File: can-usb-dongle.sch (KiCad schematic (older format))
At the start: 39 parts, among them SW1 SW_PUSH, U1 STM32F302C8T, U2 SN65HVD256, U3 MCP1700, U4 SiP32431, X1 16MHz 10ppm

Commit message: Rearrange symbols.
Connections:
- wire segments 129 -> 128
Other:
- moved on the sheet: C10, C7, C8, C9, C?, CONN1, CONN2, CONN?, D2, D3, D?, F1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

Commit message: Start with footrpint placement on PCB
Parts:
- removed CONN2: UART, symbol UART
- added CONN1: UART, _connectors:Molex-PicoBlade-4, symbol CONN_01X04
- added R10, R11: 100, _std:_0603, symbol R
- C1, C2, C3, C4, C6, C7, C8: footprint Capacitors_SMD:C_0603_HandSoldering -> _std:_0603
- C10, C13, C14, C9: renamed from C?; footprint (none) -> _std:_0603
- C11: renamed from C9; footprint Capacitors_SMD:C_0603_HandSoldering -> _std:_0603
- C12: renamed from C10; footprint Capacitors_SMD:C_0603_HandSoldering -> _std:_0603
- C5: value 100n -> 100nF; footprint Capacitors_SMD:C_0603_HandSoldering -> _std:_0603
- CONN2: renamed from CONN1; footprint (none) -> _connectors:_Solder_Pad1.27_5
- CONN3: renamed from CONN?; footprint (none) -> _connectors:_Micro-USB-AB-receptacle-SMT-th
- CONN4: renamed from CONN3; footprint Connectors_Molex:Connector_Molex_PicoBlade_53261-0471 -> _connectors:_Molex-PicoBlade-SMD-4
- CONN5: renamed from CONN4; footprint Connectors_Molex:Connector_Molex_PicoBlade_53261-0471 -> _connectors:_Molex-PicoBlade-SMD-4
- D1: renamed from D2; footprint LEDs:LED-0603 -> _std:_0603
- D2: renamed from D3; footprint LEDs:LED-0603 -> _std:_0603
- D3: renamed from D?; footprint LEDs:LED-0603 -> _std:_0603
- F1: footprint Resistors_SMD:R_0805_HandSoldering -> _std:_0603
- R1, R2, R5, R6: footprint Resistors_SMD:R_0603 -> _std:_0603
- R3, R4, R8: renamed from R?; footprint (none) -> _std:_0603
- R7: renamed from R?; footprint Resistors_SMD:R_0603 -> _std:_0603
- R9: renamed from R7; footprint Resistors_SMD:R_0603 -> _std:_0603
- SW1: footprint (none) -> _div:PushButtonSMD-5x3mm
- U2: footprint Transistors_SMD:sc70-5 -> Housings_SOIC:SOIC-8_3.9x4.9mm_Pitch1.27mm
- U3: renamed from U?; footprint (none) -> _std:SOT-563_6-lead
- U5: renamed from U4; footprint (none) -> Housings_SOT-23_SOT-143_TSOT-6:SC-70-6
- X1: footprint (none) -> _div:_TSX-3225-SMD-XTAL
- renumbered U3 to U4
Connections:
- wire segments 128 -> 100
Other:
- note added: "(5V tolerant)"
- note removed: "5V tolerant"
- note removed: "PREVIEW VERSION!\nPINOUT CAN CHANGE"

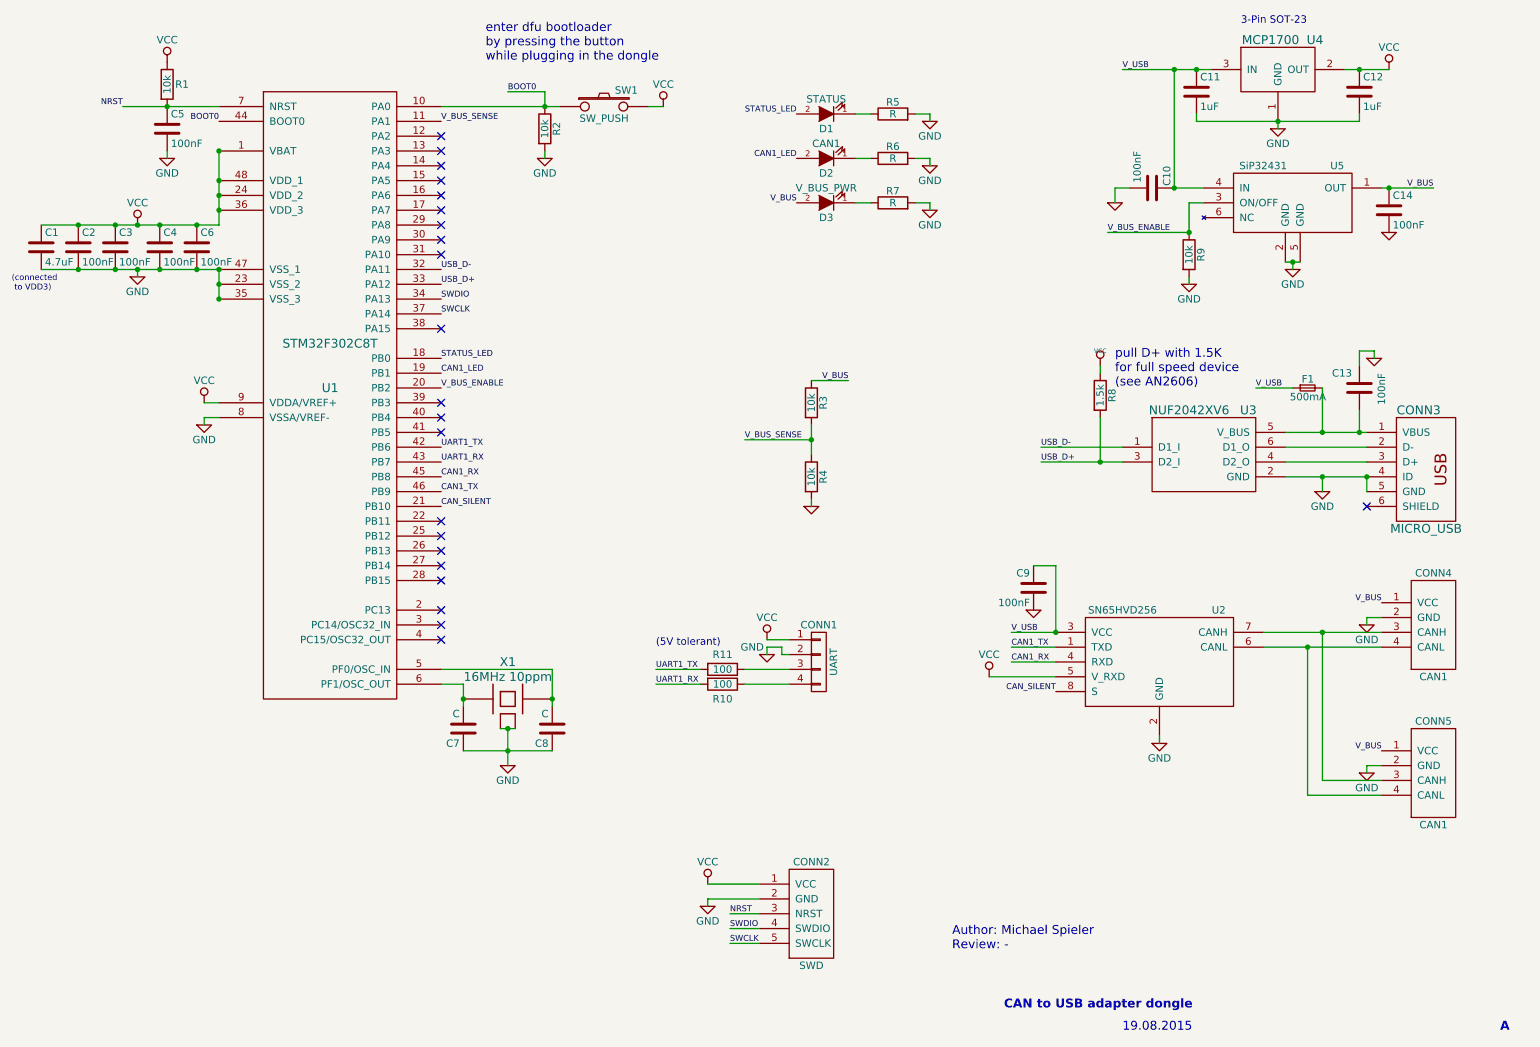
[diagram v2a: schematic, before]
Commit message: Most components placed.
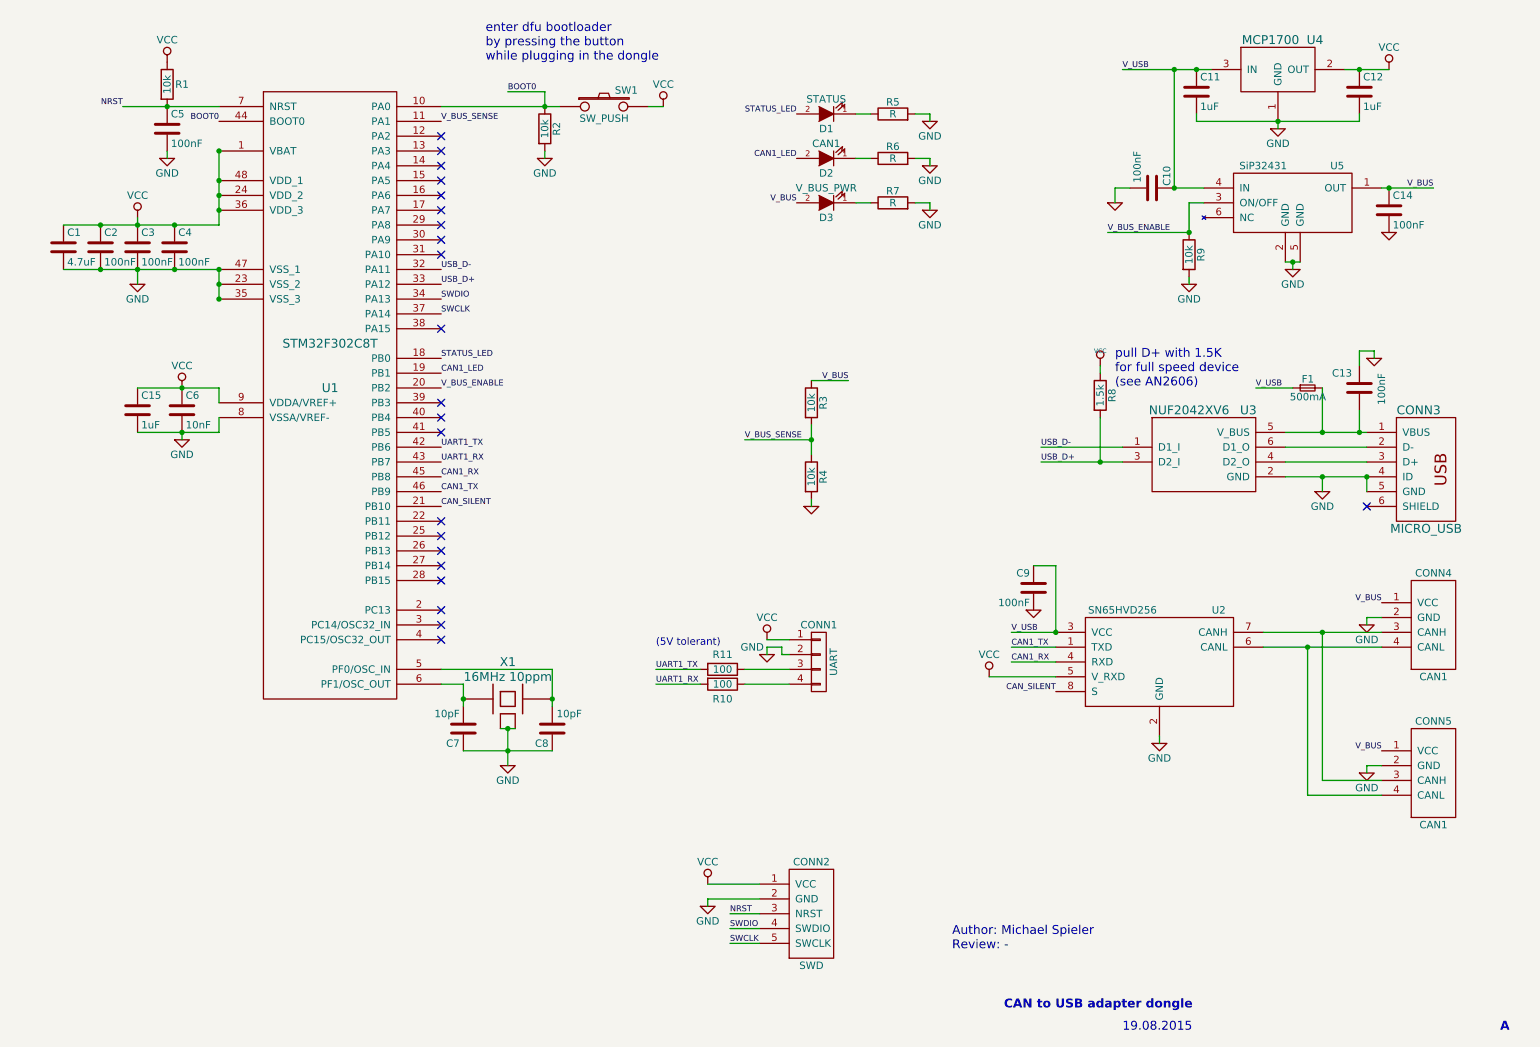
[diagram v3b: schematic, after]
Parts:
- added C15: 1uF, _std:_0603, symbol C
- C6: value 100nF -> 10nF
- C7, C8: value C -> 10pF
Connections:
- net GND: now also C15.2
- net VCC: now also C15.1
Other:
- note removed: "(connected\n to VDD3)"
- note removed: "3-Pin SOT-23"
- moved on the sheet: C1, C2, C3, C4, C6
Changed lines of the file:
@@
 L GND-RESCUE-can-usb-dongle #PWR01
 U 1 1 5561F00A
-P 1550 2550
-F 0 "#PWR01" H 1550 2300 50  0001 C CNN
-F 1 "GND" H 1550 2450 50  0000 C CNN
-F 2 "" H 1550 2550 60  0000 C CNN
-F 3 "" H 1550 2550 60  0000 C CNN
-	1    1550 2550
+P 1550 2600
+F 0 "#PWR01" H 1550 2350 50  0001 C CNN
+F 1 "GND" H 1550 2500 50  0000 C CNN
+F 2 "" H 1550 2600 60  0000 C CNN
+F 3 "" H 1550 2600 60  0000 C CNN
+	1    1550 2600
 	1    0    0    -1
 $EndComp
@@
 L VCC #PWR02
 U 1 1 5561F01F
-P 1550 2200
-F 0 "#PWR02" H 1550 2050 50  0001 C CNN
-F 1 "VCC" H 1550 2350 50  0000 C CNN
-F 2 "" H 1550 2200 60  0000 C CNN
-F 3 "" H 1550 2200 60  0000 C CNN
-	1    1550 2200
+P 1550 2150
+F 0 "#PWR02" H 1550 2000 50  0001 C CNN
+F 1 "VCC" H 1550 2300 50  0000 C CNN
+F 2 "" H 1550 2150 60  0000 C CNN
+F 3 "" H 1550 2150 60  0000 C CNN
+	1    1550 2150
 	1    0    0    -1
 $EndComp
@@
 L C C6
 U 1 1 5561F0D0
-P 1950 2350
-F 0 "C6" H 1975 2450 50  0000 L CNN
-F 1 "100nF" H 1975 2250 50  0000 L CNN
-F 2 "_std:_0603" H 1988 2200 30  0001 C CNN
-F 3 "" H 1950 2350 60  0000 C CNN
-	1    1950 2350
+P 1850 3450
+F 0 "C6" H 1875 3550 50  0000 L CNN
+F 1 "10nF" H 1875 3350 50  0000 L CNN
+F 2 "_std:_0603" H 1888 3300 30  0001 C CNN
+F 3 "" H 1850 3450 60  0000 C CNN
+	1    1850 3450
 	1    0    0    -1
 $EndComp
@@
 L C C4
 U 1 1 5561F0E9
-P 1700 2350
-F 0 "C4" H 1725 2450 50  0000 L CNN
-F 1 "100nF" H 1725 2250 50  0000 L CNN
-F 2 "_std:_0603" H 1738 2200 30  0001 C CNN
-F 3 "" H 1700 2350 60  0000 C CNN
-	1    1700 2350
+P 1800 2350
+F 0 "C4" H 1825 2450 50  0000 L CNN
+F 1 "100nF" H 1825 2250 50  0000 L CNN
+F 2 "_std:_0603" H 1838 2200 30  0001 C CNN
+F 3 "" H 1800 2350 60  0000 C CNN
+	1    1800 2350
 	1    0    0    -1
 $EndComp
@@
 L C C3
 U 1 1 5561F104
-P 1400 2350
-F 0 "C3" H 1425 2450 50  0000 L CNN
-F 1 "100nF" H 1425 2250 50  0000 L CNN
-F 2 "_std:_0603" H 1438 2200 30  0001 C CNN
-F 3 "" H 1400 2350 60  0000 C CNN
-	1    1400 2350
+P 1550 2350
+F 0 "C3" H 1575 2450 50  0000 L CNN
+F 1 "100nF" H 1575 2250 50  0000 L CNN
+F 2 "_std:_0603" H 1588 2200 30  0001 C CNN
+F 3 "" H 1550 2350 60  0000 C CNN
+	1    1550 2350
 	1    0    0    -1
 $EndComp
@@
 L C C2
 U 1 1 5561F125
-P 1150 2350
-F 0 "C2" H 1175 2450 50  0000 L CNN
-F 1 "100nF" H 1175 2250 50  0000 L CNN
-F 2 "_std:_0603" H 1188 2200 30  0001 C CNN
-F 3 "" H 1150 2350 60  0000 C CNN
-	1    1150 2350
+P 1300 2350
+F 0 "C2" H 1325 2450 50  0000 L CNN
+F 1 "100nF" H 1325 2250 50  0000 L CNN
+F 2 "_std:_0603" H 1338 2200 30  0001 C CNN
+F 3 "" H 1300 2350 60  0000 C CNN
+	1    1300 2350
 	1    0    0    -1
 $EndComp
@@
 L C C1
 U 1 1 5561F145
-P 900 2350
-F 0 "C1" H 925 2450 50  0000 L CNN
-F 1 "4.7uF" H 925 2250 50  0000 L CNN
-F 2 "_std:_0603" H 938 2200 30  0001 C CNN
-F 3 "" H 900 2350 60  0000 C CNN
-	1    900  2350
+P 1050 2350
+F 0 "C1" H 1075 2450 50  0000 L CNN
+F 1 "4.7uF" H 1075 2250 50  0000 L CNN
+F 2 "_std:_0603" H 1088 2200 30  0001 C CNN
+F 3 "" H 1050 2350 60  0000 C CNN
+	1    1050 2350
 	1    0    0    -1
 $EndComp
@@
 L GND-RESCUE-can-usb-dongle #PWR03
 U 1 1 5561F50D
-P 2000 3550
-F 0 "#PWR03" H 2000 3300 50  0001 C CNN
-F 1 "GND" H 2000 3450 50  0000 C CNN
-F 2 "" H 2000 3550 60  0000 C CNN
-F 3 "" H 2000 3550 60  0000 C CNN
-	1    2000 3550
+P 1850 3650
+F 0 "#PWR03" H 1850 3400 50  0001 C CNN
+F 1 "GND" H 1850 3550 50  0000 C CNN
+F 2 "" H 1850 3650 60  0000 C CNN
+F 3 "" H 1850 3650 60  0000 C CNN
+	1    1850 3650
 	1    0    0    -1
 $EndComp
@@
 L VCC #PWR04
 U 1 1 5561F52B
-P 2000 3400
-F 0 "#PWR04" H 2000 3250 50  0001 C CNN
-F 1 "VCC" H 2000 3550 50  0000 C CNN
-F 2 "" H 2000 3400 60  0000 C CNN
-F 3 "" H 2000 3400 60  0000 C CNN
-	1    2000 3400
+P 1850 3300
+F 0 "#PWR04" H 1850 3150 50  0001 C CNN
+F 1 "VCC" H 1850 3450 50  0000 C CNN
+F 2 "" H 1850 3300 60  0000 C CNN
+F 3 "" H 1850 3300 60  0000 C CNN
+	1    1850 3300
 	1    0    0    -1
 $EndComp
@@
 P 4350 5600
 F 0 "C8" H 4375 5700 50  0000 L CNN
-F 1 "C" H 4375 5500 50  0000 L CNN
+F 1 "10pF" H 4150 5500 50  0000 L CNN
 F 2 "_std:_0603" H 4388 5450 30  0001 C CNN
 F 3 "" H 4350 5600 60  0000 C CNN
@@
 P 3750 5600
 F 0 "C7" H 3775 5700 50  0000 L CNN
-F 1 "C" H 3775 5500 50  0000 L CNN
+F 1 "10pF" H 3775 5500 50  0000 L CNN
 F 2 "_std:_0603" H 3788 5450 30  0001 C CNN
 F 3 "" H 3750 5600 60  0000 C CNN
@@
 Text Label 3600 3200 0    40   ~ 0
 CAN1_LED
-Text Notes 700  2650 0    40   ~ 0
-(connected\n to VDD3)
 $Comp
 L LED D2
@@
 NoConn ~ 3600 1700
 NoConn ~ 3600 1600
-Text Notes 9000 850  0    50   ~ 0
-3-Pin SOT-23
 $Comp
 L CAN CONN5
@@
 Wire Wire Line
 	1450 1400 2100 1400
-Wire Wire Line
-	2000 3500 2100 3500
-Wire Wire Line
-	2000 3400 2100 3400
-Connection ~ 1950 2500
-Connection ~ 1700 2500
-Connection ~ 1150 2500
-Connection ~ 1400 2500
+Connection ~ 1800 2500
+Connection ~ 1300 2500
 Connection ~ 1550 2500
-Wire Wire Line
-	900  2500 2100 2500
-Connection ~ 1950 2200
-Connection ~ 1700 2200
+Connection ~ 1800 2200
 Connection ~ 1550 2200
-Connection ~ 1400 2200
-Connection ~ 1150 2200
-Wire Wire Line
-	2100 2200 900  2200
+Connection ~ 1300 2200
 Wire Wire Line
 	6800 1450 6900 1450
@@
 	5000 1400 5100 1400
 Wire Wire Line
-	2100 1700 2100 2200
+	2100 2200 2100 1700
 Wire Wire Line
 	2100 2500 2100 2700
@@
 Wire Wire Line
 	1750 1750 1750 1700
-Wire Wire Line
-	1550 2550 1550 2500
-Wire Wire Line
-	2000 3550 2000 3500
 Wire Wire Line
 	5400 6750 5400 6800
@@
 Wire Wire Line
 	5900 5100 5950 5100
+Wire Wire Line
+	1550 2500 1550 2600
+Wire Wire Line
+	1050 2200 2100 2200
+Wire Wire Line
+	1050 2500 2100 2500
+Wire Wire Line
+	1550 2150 1550 2200
+$Comp
+L C C15
+U 1 1 562609FA
+P 1550 3450
+F 0 "C15" H 1575 3550 50  0000 L CNN
+F 1 "1uF" H 1575 3350 50  0000 L CNN
+F 2 "_std:_0603" H 1588 3300 30  0001 C CNN
+F 3 "" H 1550 3450 60  0000 C CNN
+	1    1550 3450
+	1    0    0    -1
+$EndComp
+Wire Wire Line
+	1550 3600 2100 3600
+Wire Wire Line
+	2100 3600 2100 3500
+Wire Wire Line
+	2100 3300 2100 3400
+Wire Wire Line
+	1550 3300 2100 3300
+Connection ~ 1850 3300
+Connection ~ 1850 3600
+Wire Wire Line
+	1850 3600 1850 3650
 $EndSCHEMATC

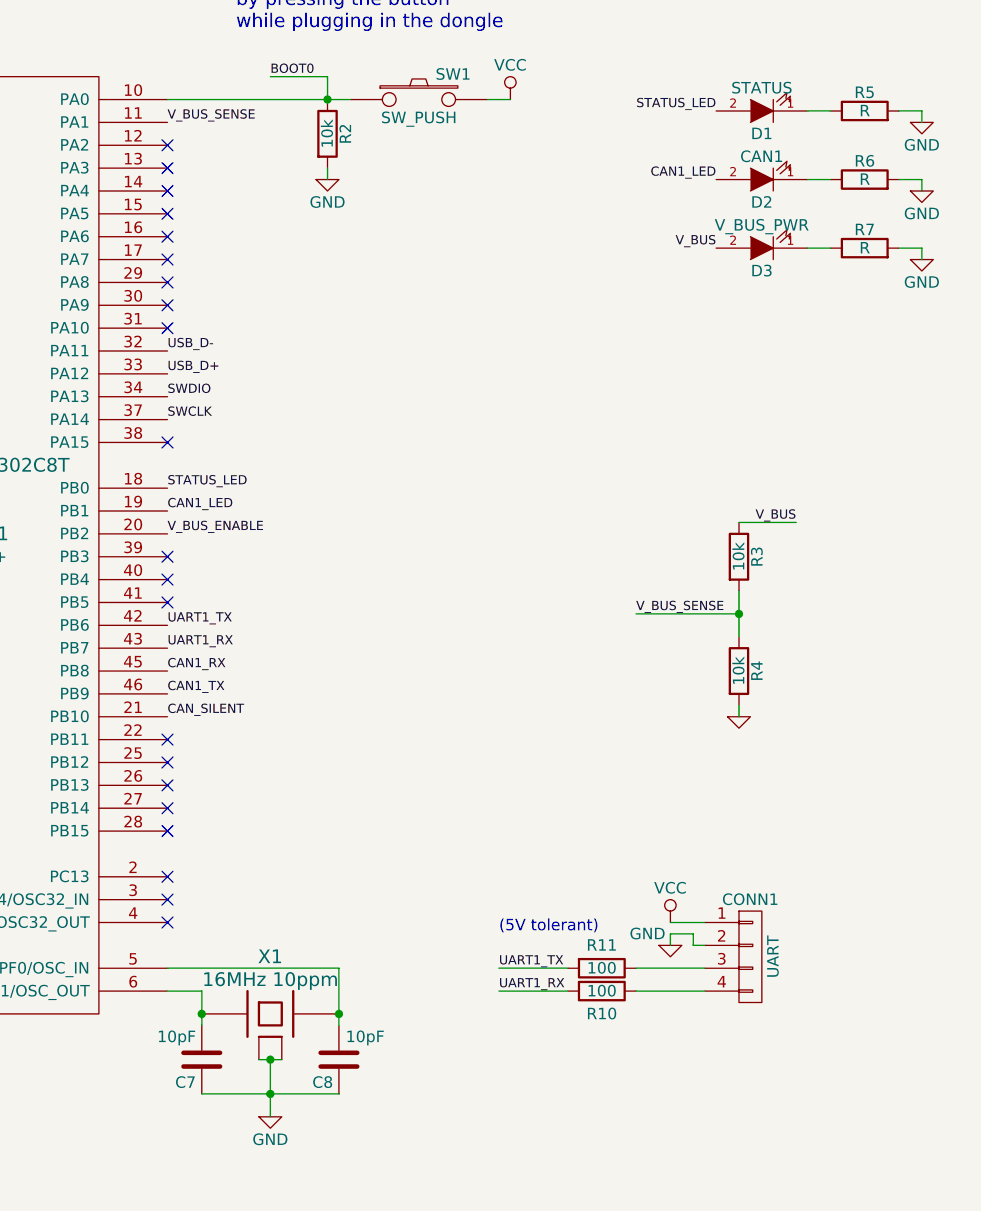
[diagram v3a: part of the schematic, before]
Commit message: Connect CAN bus power LED to GPIO, update connector footprints.
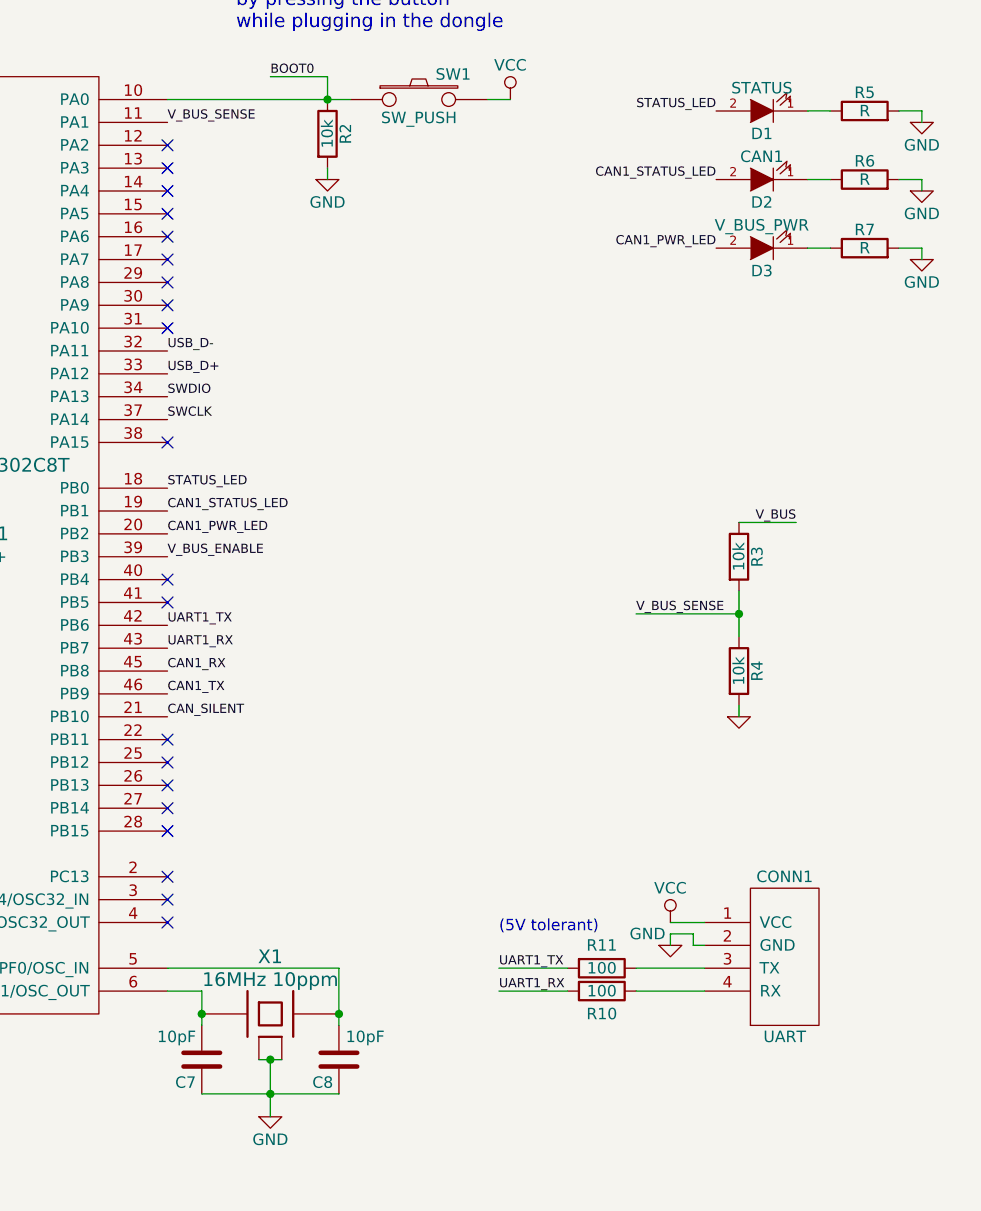
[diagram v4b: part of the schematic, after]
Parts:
- removed CONN1: UART, _connectors:Molex-PicoBlade-4, symbol CONN_01X04
- added CONN1: UART, _connectors:Molex-PicoBlade-4, symbol UART
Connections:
- net GND: now also CONN1.2 (GND), CONN1.MECH (GND)
- net VCC: now also CONN1.1 (VCC)
- net V_BUS: no longer D3.2 (A)
- net V_BUS_ENABLE: now also U1.39 (PB3); no longer U1.20 (PB2)
- net at R10.1: now also CONN1.4 (RX)
- net at R11.1: now also CONN1.3 (TX)
- net CAN1_LED renamed CAN1_STATUS_LED
- new net CAN1_PWR_LED: D3.2 (A), U1.20 (PB2)
- no-connect marks 22 -> 21
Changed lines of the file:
@@
 Text Label 6000 1450 2    40   ~ 0
 STATUS_LED
-Text Label 6000 1750 2    40   ~ 0
-CAN1_LED
 Text Label 3600 3200 0    40   ~ 0
-CAN1_LED
+CAN1_STATUS_LED
 $Comp
 L LED D2
@@
 Text Label 8100 2250 0    40   ~ 0
 V_BUS_ENABLE
-Text Label 3600 3300 0    40   ~ 0
+Text Label 3600 3400 0    40   ~ 0
 V_BUS_ENABLE
 $Comp
@@
 	1    0    0    -1
 $EndComp
-Text Label 6000 2050 2    40   ~ 0
-V_BUS
 Text Label 6350 3250 2    40   ~ 0
 V_BUS
@@
 NoConn ~ 3600 3600
 NoConn ~ 3600 3500
-NoConn ~ 3600 3400
 NoConn ~ 3600 2900
 NoConn ~ 3600 2200
@@
 Wire Wire Line
 	5950 5200 5650 5200
-$Comp
-L CONN_01X04 CONN1
-U 1 1 56255440
-P 6150 5150
-F 0 "CONN1" H 6150 5400 50  0000 C CNN
-F 1 "UART" V 6250 5150 50  0000 C CNN
-F 2 "_connectors:Molex-PicoBlade-4" H 6150 5150 60  0001 C CNN
-F 3 "" H 6150 5150 60  0000 C CNN
-	1    6150 5150
-	1    0    0    -1
-$EndComp
 Wire Wire Line
 	5800 5100 5800 5050
@@
 Wire Wire Line
 	1850 3600 1850 3650
+Text Label 6000 2050 2    40   ~ 0
+CAN1_PWR_LED
+Text Label 3600 3300 0    40   ~ 0
+CAN1_PWR_LED
+Text Label 6000 1750 2    40   ~ 0
+CAN1_STATUS_LED
+$Comp
+L UART CONN1
+U 1 1 5626A8AF
+P 6300 5150
+F 0 "CONN1" H 6300 5500 50  0000 C CNN
+F 1 "UART" H 6300 4800 50  0000 C CNN
+F 2 "_connectors:Molex-PicoBlade-4" H 6300 5150 50  0001 C CNN
+F 3 "DOCUMENTATION" H 6300 5150 50  0001 C CNN
+	1    6300 5150
+	1    0    0    -1
+$EndComp
 $EndSCHEMATC
